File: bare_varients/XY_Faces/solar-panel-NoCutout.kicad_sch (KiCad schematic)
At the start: 25 parts, among them J1 CON-5040500591, J2 Conn_01x01, J3 Conn_01x01, J4 Conn_01x01, J5 Conn_01x01, U1 VEML7700, U2 MCP9808_DFN, U3 DRV2605LDGS

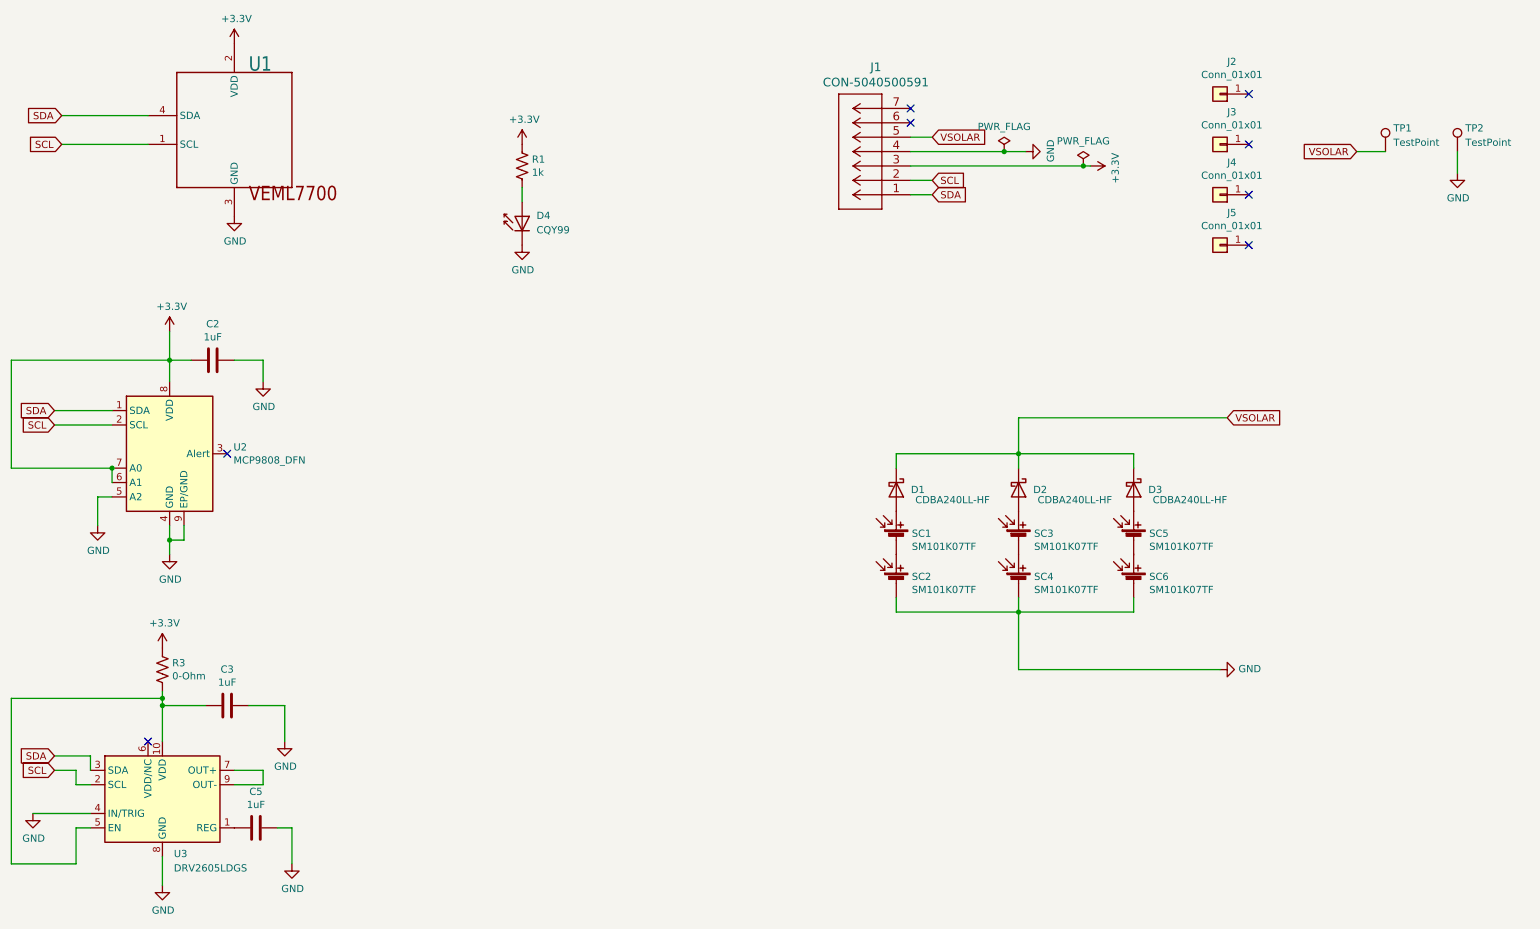
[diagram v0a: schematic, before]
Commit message: Adjusted Solar Board
Changed temperature sensor footprint from DFM to MSOP
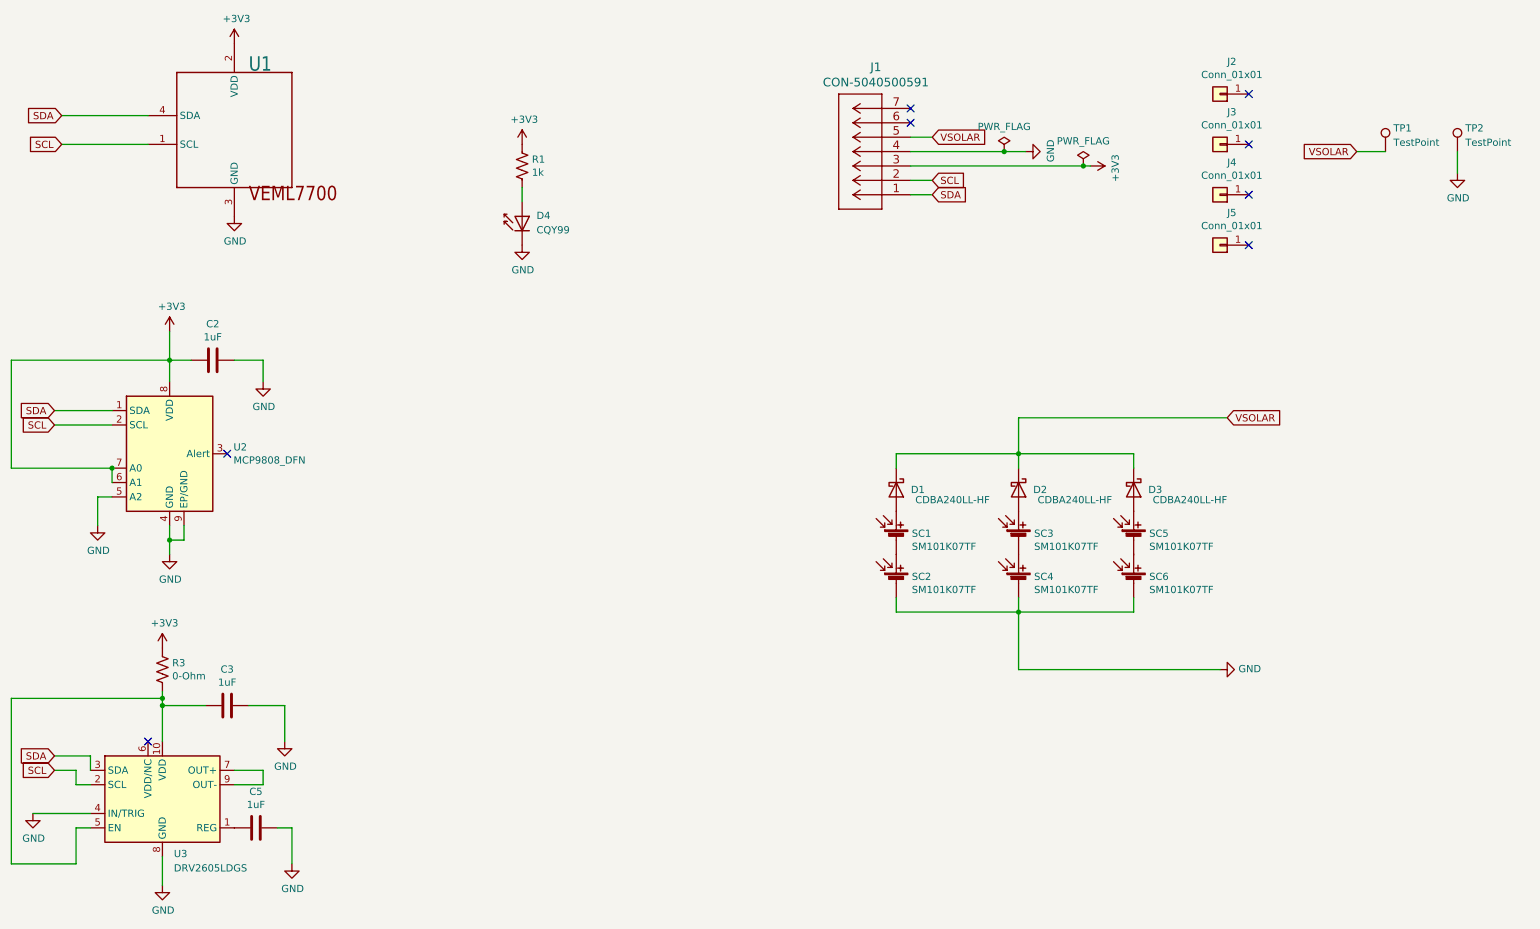
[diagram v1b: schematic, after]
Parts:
- U2: footprint SolarPanelBoards:MCP9808-NoLeadPackage -> Package_SO:MSOP-8-1EP_3x3mm_P0.65mm_EP1.5x1.8mm_ThermalVias
